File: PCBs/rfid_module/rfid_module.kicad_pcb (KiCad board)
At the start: 2 copper layers, 15.8 x 12 mm, 47 parts, among them IC201 TLV9004SIRTER, IC202 MAX9027EBT+T, Q201 DMN21D2UFB-7B, Q202 DMP21D5UFB4-7B, Q203 DMN21D2UFB-7B, Q204 DMN21D2UFB-7B

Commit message: RFID Module progress
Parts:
- added C301: 4u7, Capacitor_SMD:C_0402_1005Metric, F.Cu at (114.4, 60.9)
- added C302: 100n, Capacitor_SMD:C_0402_1005Metric, F.Cu at (113.0, 61.9)
- added C303: 1u, Capacitor_SMD:C_0402_1005Metric, B.Cu at (114.5, 60.9)
- added C304: 100n, Capacitor_SMD:C_0402_1005Metric, B.Cu at (114.5, 59.9)
- added C501: 22u, Capacitor_SMD:C_0402_1005Metric, F.Cu at (115.4, 57.7)
- added C502: 4u7, Capacitor_SMD:C_0402_1005Metric, F.Cu at (112.0, 55.9)
- added IC501: MAX17291BANT+T, watch_footprints:BGA6C40P3X2_127X87X50, F.Cu at (113.6, 56.0)
- added J401: 10-Pin_Pogo_Connector_Male, watch_footprints:10-Pin Pogo Connector Male, B.Cu at (109.6, 60.4)
- added L501: 10u, Inductor_SMD:L_TDK_MLZ1608, F.Cu at (115.4, 56.0)
- added Q401: DMN21D2UFB-7B, watch_footprints:DMN21D2UFB7B, F.Cu at (114.4, 59.9)
- added R401: 10k, Resistor_SMD:R_0402_1005Metric, F.Cu at (114.4, 58.8)
- added R402: 100k, Resistor_SMD:R_0402_1005Metric, B.Cu at (114.5, 58.4)
- added R501: 3M48, Resistor_SMD:R_0402_1005Metric, F.Cu at (110.8, 55.9)
- added R502: 402k, Resistor_SMD:R_0402_1005Metric, F.Cu at (113.4, 57.7)
- added R503: 1M, Resistor_SMD:R_0402_1005Metric, F.Cu at (111.4, 57.7)
- added R504: 100k, Resistor_SMD:R_0402_1005Metric, F.Cu at (135.4, 54.9)
- added U101: Watch_Module_Outline_V1, watch_footprints:Watch Module Outline V1, F.Cu at (105.0, 62.0)
- added U301: STM32G071G8Ux, Package_DFN_QFN:QFN-28_4x4mm_P0.5mm, F.Cu at (109.8, 61.4)
- R206: value 4R7 -> 100R
- R207: value 4R7 -> 10k
- moved Q203 64.1 mm to (107.0, 55.8), turned to -90 degrees
- moved Q202 61.5 mm to (108.4, 55.8), turned to -90 degrees
- moved Q201 58.0 mm to (109.5, 57.7), turned to 180 degrees
- moved R206 46.0 mm to (106.9, 57.7), turned to 90 degrees
- moved R204 42.5 mm to (109.6, 55.9), turned to 90 degrees
- moved R202 40.2 mm to (108.0, 57.7), turned to 90 degrees
- moved R201 39.8 mm to (106.2, 59.3)
- moved R207 39.6 mm to (114.5, 52.1), turned to 90 degrees
- moved L201 35.2 mm to (100.0, 56.5), turned to 180 degrees
- moved IC201 34.6 mm to (99.3, 64.1)
- moved IC202 22.1 mm to (151.2, 73.8)
- moved Q204 22.1 mm to (161.9, 76.6)
- moved R212 22.1 mm to (148.6, 67.0)
- moved R213 22.1 mm to (151.5, 57.0)
- moved R218 22.1 mm to (151.5, 67.0)
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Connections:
- net +VSYS renamed /Boost Converter/VRF
- Q201 pad 3: /RFID/SHIFT_G -> /RFID/GATE
- Q202 pad 1: /RFID/SHIFT_PD -> /RFID/OUT_SHIFT
- Q202 pad 2: /RFID/SHIFT_G -> /RFID/GATE
- Q203 pad 1: /RFID/SHIFT_G -> /RFID/OUTN_G
- Q203 pad 3: /RFID/SHIFT_ND -> /RFID/OUT_SHIFT
- R201 pad 2: /RFID/OUT -> /RFID/OUTN
- R202 pad 1: /RFID/OUT -> /RFID/OUTN
- R202 pad 2: /RFID/OUT_G -> /RFID/OUTN_G
- R204 pad 1: /RFID/SHIFT_G -> /RFID/GATE
- R206 pad 1: /RFID/OUT_SHIFT -> /RFID/OUT
- R206 pad 2: /RFID/SHIFT_PD -> /RFID/OUT_G
- R207 pad 1: /RFID/SHIFT_ND -> /RFID/OUT
- R207 pad 2: /RFID/OUT_SHIFT -> +3V3
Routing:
- net GND: track 0.00 -> 7.53 mm, vias 0 -> 6
- net /Boost Converter/EN: track 0.00 -> 5.92 mm
- net /Pogo Connector/LPUART1_RX: track 0.00 -> 5.55 mm, vias 0 -> 1
- net /Pogo Connector/LPUART1_RX_1V8: track 0.00 -> 5.40 mm, vias 0 -> 1
- net +1V8: track 0.00 -> 4.29 mm, vias 0 -> 1
- net /Boost Converter/FB: track 0.00 -> 4.24 mm
- net /RFID/OUT: track 0.00 -> 3.85 mm
- net /RFID/OUTN: track 0.00 -> 3.62 mm
- net /RFID/GATE: track 0.00 -> 3.38 mm
- net +3V3: track 0.00 -> 3.20 mm, vias 0 -> 3
- net /RFID/OUT_G: track 0.00 -> 2.55 mm
- net /Boost Converter/FB_OFFSET: track 0.00 -> 2.27 mm
- net /RFID/OUTN_G: track 0.00 -> 1.86 mm
- net /Pogo Connector/LPUART1_TX: track 0.00 -> 1.64 mm, vias 0 -> 1
- net /STM32G0/NRST: track 0.00 -> 1.59 mm, vias 0 -> 1
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- added copper zone on In1.Cu, net GND
- added copper zone on In3.Cu, net GND
- added copper zone on In6.Cu, net GND
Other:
- board size 15.8 x 12 mm -> 22.5 x 14.5 mm
- copper layers 2 -> 8

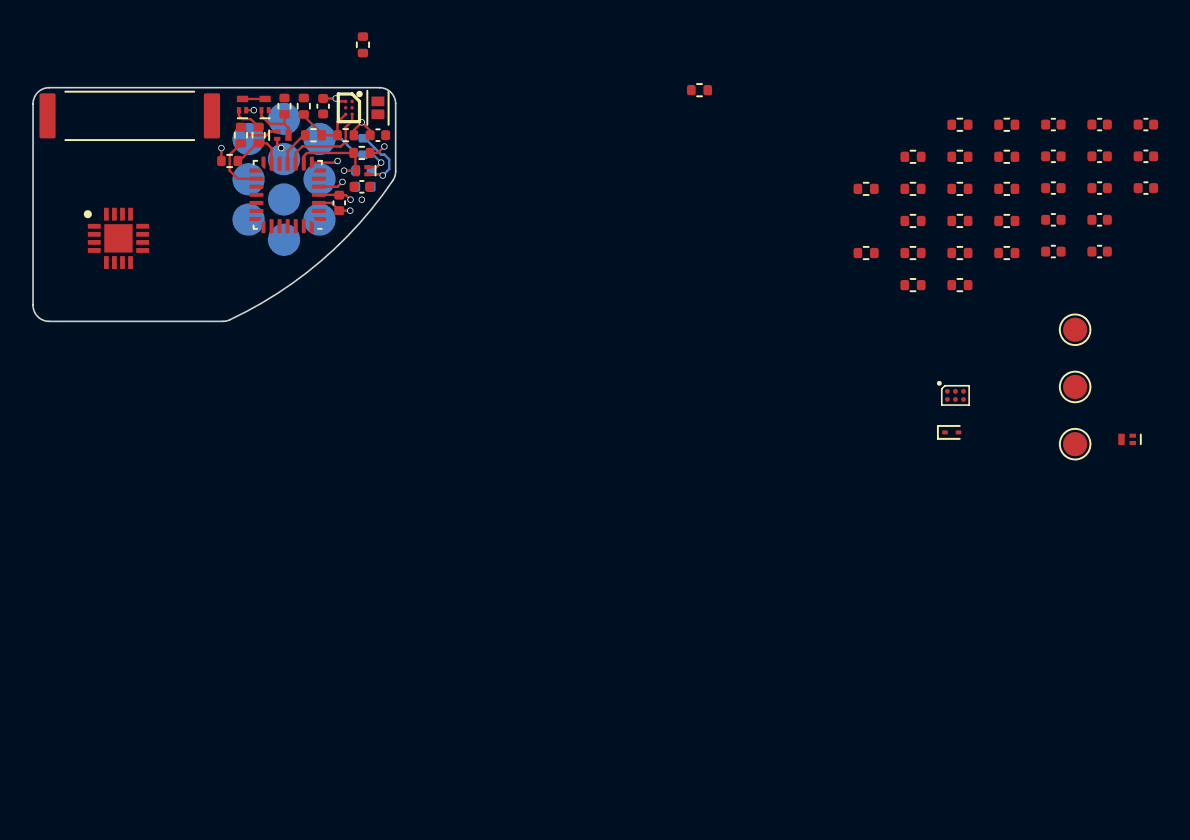
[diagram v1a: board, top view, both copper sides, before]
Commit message: RFID PCB Done, started lower flex PCB
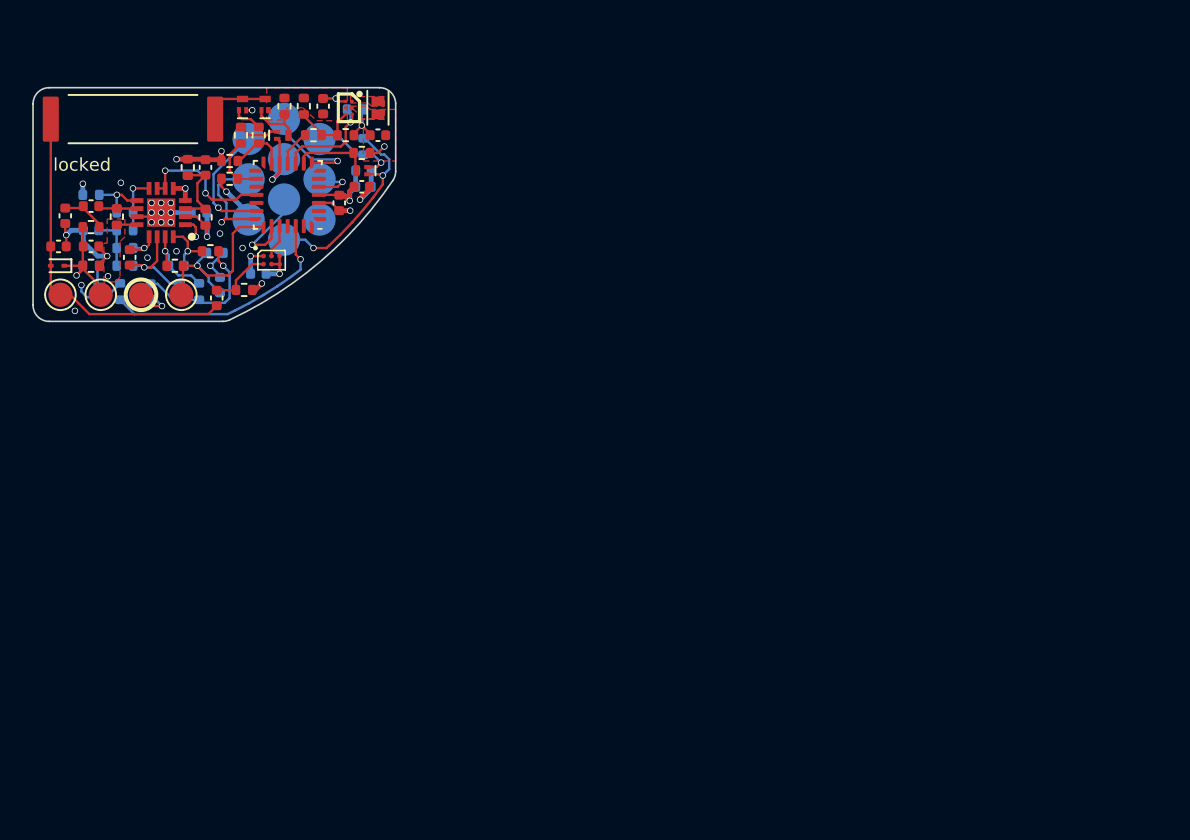
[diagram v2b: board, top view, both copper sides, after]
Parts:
- added TP101: 1.5mm, TestPoint:TestPoint_Pad_D1.5mm, F.Cu at (100.7, 67.6)
- C203, C206, C210, C211, C212, C213, Q204, R208, R209, R210, R213, R214, R215, R216, R218, R220, R223, R504: moved to B.Cu
- moved Q204 64.4 mm to (98.1, 67.4), turned to -90 degrees
- moved TP201 63.0 mm to (95.7, 67.6)
- moved C206 62.9 mm to (97.6, 63.6), turned to 180 degrees
- moved C207 62.8 mm to (97.6, 64.6)
- moved C205 61.7 mm to (95.6, 64.6)
- moved C201 61.6 mm to (96.0, 62.7), turned to -90 degrees
- moved TP202 60.7 mm to (98.2, 67.6)
- moved C212 60.5 mm to (102.9, 65.8)
- moved C208 60.3 mm to (100.0, 65.3), turned to 90 degrees
- moved C202 59.8 mm to (97.6, 62.1)
- moved C210 58.9 mm to (101.3, 67.4), turned to -90 degrees
- moved C213 57.8 mm to (105.6, 67.0), turned to 90 degrees
- moved D201 56.4 mm to (95.5, 65.8), turned to 180 degrees
- moved TP203 56.2 mm to (103.2, 67.6)
- moved C211 55.8 mm to (108.0, 66.3)
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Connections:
- C211 pad 1: +1V8 -> +3V3
- IC202 pad A1: +1V8 -> +3V3
- J401 pad A1: unconnected-(J401-PadA1) -> /Pogo Connector/SWDIO
- J401 pad A2: unconnected-(J401-PadA2) -> /Pogo Connector/SWCLK
- J401 pad B3: unconnected-(J401-PadB3) -> /Pogo Connector/IRQN
- J401 pad B4: +1V8 -> IOREF
- J401 pad C2: unconnected-(J401-PadC2) -> /Pogo Connector/NRST
- Q401 pad 1: +1V8 -> IOREF
- R402 pad 1: +1V8 -> IOREF
- U301 pad 12: unconnected-(U301-PA6-Pad12) -> GND
- U301 pad 18: unconnected-(U301-PA11/PA9-Pad18) -> /RFID/SHDN
- U301 pad 20: /STM32G0/SWDIO -> /Pogo Connector/SWDIO
- U301 pad 21: /STM32G0/SWCLK -> /Pogo Connector/SWCLK
- U301 pad 23: unconnected-(U301-PB3-Pad23) -> /Pogo Connector/IRQN
- U301 pad 26: unconnected-(U301-PB6-Pad26) -> /RFID/PULL
- U301 pad 5: /STM32G0/NRST -> /Pogo Connector/NRST
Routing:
- net GND: track 7.53 -> 36.2 mm, vias 6 -> 29
- net /RFID/RF: track 0.00 -> 21.8 mm
- net /RFID/PULL: track 0.00 -> 15.2 mm, vias 0 -> 1
- net /RFID/RF_IN: track 0.00 -> 13.0 mm, vias 0 -> 1
- net IOREF: track 0.00 -> 13.0 mm, vias 0 -> 2
- net +3V3: track 3.20 -> 15.3 mm, vias 3 -> 6
- net /RFID/AMP3_IN: track 0.00 -> 8.70 mm, vias 0 -> 1
- net /RFID/SHDN: track 0.00 -> 8.66 mm, vias 0 -> 2
- net /Pogo Connector/SWDIO: track 0.00 -> 7.74 mm, vias 0 -> 1
- net /RFID/SIGNAL_ENVELOPE: track 0.00 -> 7.36 mm, vias 0 -> 1
- net /Pogo Connector/SWCLK: track 0.00 -> 6.84 mm, vias 0 -> 1
- net /RFID/AMP2_OUT: track 0.00 -> 6.77 mm, vias 0 -> 1
- net /Pogo Connector/IRQN: track 0.00 -> 5.76 mm, vias 0 -> 1
- net /RFID/AMP3_OUT: track 0.00 -> 5.16 mm, vias 0 -> 1
- net /RFID/1V65_UNREG: track 0.00 -> 4.89 mm
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- added copper zone on F.Cu, net +1V65
- added copper zone on In2.Cu, net +1V65
- added copper zone on F.Cu, net +3V3
- added copper zone on In4.Cu, net +3V3
- added copper zone on In5.Cu, net +3V3
- added copper zone on F.Cu, net /Boost Converter/LX
- added copper zone on F.Cu, net /Boost Converter/VRF
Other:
- board text added: "locked"

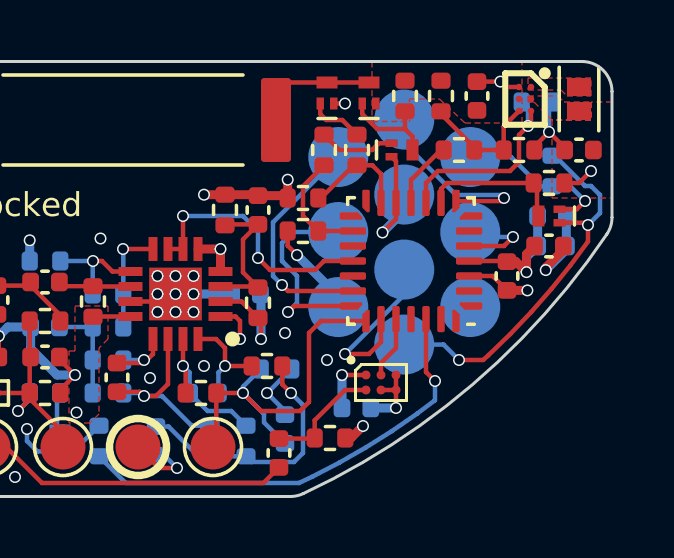
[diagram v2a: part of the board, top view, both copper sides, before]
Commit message: Flex PCB finished. Need to rotate RFID transponder coil.
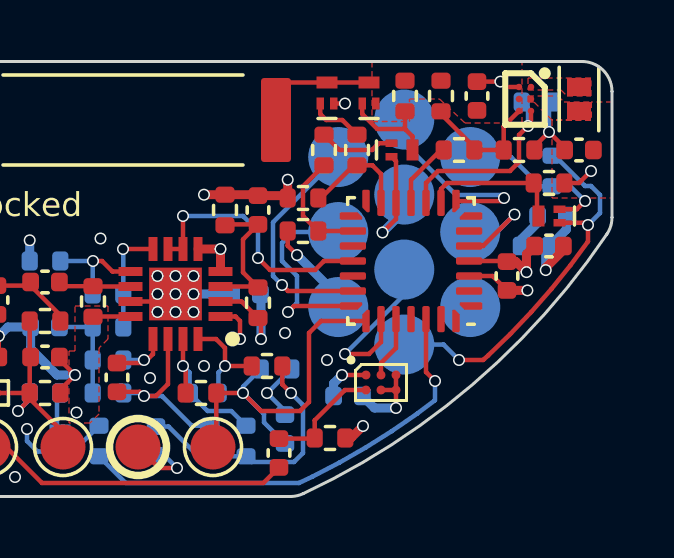
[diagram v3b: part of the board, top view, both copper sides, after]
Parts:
- moved C303 0.55 mm to (114.0, 60.9)
- moved C211 0.49 mm to (107.7, 65.9)
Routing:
- net GND: track 36.2 -> 36.8 mm
- net /Pogo Connector/NRST: track 3.08 -> 3.66 mm
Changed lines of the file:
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@@
   )
   (footprint "Capacitor_SMD:C_0402_1005Metric" locked (layer "B.Cu")
-    (at 114.5 60.9 180)
+    (at 113.95 60.9 180)
     (descr "Capacitor SMD 0402 (1005 Metric), square (rectangular) end terminal, IPC_7351 nominal, (Body size source: IPC-SM-782 page 76, https://www.pcb-3d.com/wordpress/wp-content/uploads/ipc-sm-782a_amendment_1_and_2.pdf), generated with kicad-footprint-generator")
     (tags "capacitor")
@@
   )
   (footprint "Capacitor_SMD:C_0402_1005Metric" locked (layer "B.Cu")
-    (at 107.98 66.3)
+    (at 107.7 65.9)
     (descr "Capacitor SMD 0402 (1005 Metric), square (rectangular) end terminal, IPC_7351 nominal, (Body size source: IPC-SM-782 page 76, https://www.pcb-3d.com/wordpress/wp-content/uploads/ipc-sm-782a_amendment_1_and_2.pdf), generated with kicad-footprint-generator")
     (tags "capacitor")
@@
   (via locked (at 101.95 61.9) (size 0.4) (drill 0.3) (layers "F.Cu" "B.Cu") (remove_unused_layers) (keep_end_layers) (zone_layer_connections "In1.Cu" "In3.Cu" "In6.Cu") (net 2))
   (segment locked (start 97.12 63.6) (end 96.36 63.6) (width 0.3) (layer "B.Cu") (net 2))
+  (segment locked (start 114.02 60.13) (end 114.02 59.9) (width 0.3) (layer "B.Cu") (net 2))
   (segment locked (start 97.12 63.6) (end 97.12 64.32) (width 0.3) (layer "B.Cu") (net 2))
+  (segment locked (start 113.47 60.9) (end 113.47 60.68) (width 0.3) (layer "B.Cu") (net 2))
   (segment locked (start 97 67.4) (end 97 67) (width 0.15) (layer "B.Cu") (net 2))
   (segment locked (start 97.35 67.75) (end 97 67.4) (width 0.15) (layer "B.Cu") (net 2))
@@
   (segment locked (start 101.3 67.88) (end 101.58 67.88) (width 0.15) (layer "B.Cu") (net 2))
   (segment locked (start 114.4 56.21) (end 114.51 56.1) (width 0.15) (layer "B.Cu") (net 2))
+  (segment locked (start 108.18 65.9) (end 108.58 66.3) (width 0.3) (layer "B.Cu") (net 2))
   (segment locked (start 101.58 67.88) (end 102 68.3) (width 0.15) (layer "B.Cu") (net 2))
-  (segment locked (start 108.46 66.3) (end 109.3 66.3) (width 0.3) (layer "B.Cu") (net 2))
   (segment locked (start 105 65.8) (end 105.01 65.8) (width 0.15) (layer "B.Cu") (net 2))
-  (segment locked (start 113.649 61.271) (end 114.02 60.9) (width 0.3) (layer "B.Cu") (net 2))
-  (segment locked (start 114.02 59.9) (end 114.02 60.9) (width 0.3) (layer "B.Cu") (net 2))
-  (segment locked (start 113.649 61.771) (end 113.649 61.271) (width 0.3) (layer "B.Cu") (net 2))
   (segment locked (start 109.575 59.725) (end 109.575 59.185) (width 0.3) (layer "B.Cu") (net 2))
+  (segment locked (start 113.649 61.079) (end 113.47 60.9) (width 0.3) (layer "B.Cu") (net 2))
   (segment locked (start 97.875 67.75) (end 97.35 67.75) (width 0.15) (layer "B.Cu") (net 2))
   (segment locked (start 103.82 62.5) (end 102.55 62.5) (width 0.3) (layer "B.Cu") (net 2))
+  (segment locked (start 113.649 61.771) (end 113.649 61.079) (width 0.3) (layer "B.Cu") (net 2))
   (segment locked (start 108.85 60.45) (end 109.575 59.725) (width 0.3) (layer "B.Cu") (net 2))
   (segment locked (start 105.6 66.52) (end 105.6 66.4) (width 0.15) (layer "B.Cu") (net 2))
+  (segment locked (start 108.58 66.3) (end 109.3 66.3) (width 0.3) (layer "B.Cu") (net 2))
   (segment locked (start 105.6 66.4) (end 105 65.8) (width 0.15) (layer "B.Cu") (net 2))
   (segment locked (start 105.01 65.8) (end 105.81 65) (width 0.15) (layer "B.Cu") (net 2))
+  (segment locked (start 113.47 60.68) (end 114.02 60.13) (width 0.3) (layer "B.Cu") (net 2))
   (segment locked (start 99.21 62.25) (end 99.2 62.24) (width 0.15) (layer "F.Cu") (net 3))
   (segment locked (start 98.22 62.24) (end 98.08 62.1) (width 0.15) (layer "F.Cu") (net 3))
@@
   (via locked (at 104.8 64) (size 0.4) (drill 0.3) (layers "F.Cu" "B.Cu") (remove_unused_layers) (keep_end_layers) (zone_layer_connections "In4.Cu" "In5.Cu") (net 4))
   (via locked (at 106 61.2) (size 0.4) (drill 0.3) (layers "F.Cu" "B.Cu") (remove_unused_layers) (keep_end_layers) (zone_layer_connections "In4.Cu" "In5.Cu") (net 4))
-  (segment locked (start 114.98 59.9) (end 114.98 60.9) (width 0.3) (layer "B.Cu") (net 4))
+  (segment locked (start 114.291 61.703) (end 114.291 61.039) (width 0.3) (layer "B.Cu") (net 4))
+  (segment locked (start 114.98 60.35) (end 114.98 59.9) (width 0.3) (layer "B.Cu") (net 4))
+  (segment locked (start 114.291 61.039) (end 114.98 60.35) (width 0.3) (layer "B.Cu") (net 4))
   (segment locked (start 106 61.2) (end 107.375 62.575) (width 0.3) (layer "B.Cu") (net 4))
+  (segment locked (start 107.22 65.48) (end 107.5 65.2) (width 0.3) (layer "B.Cu") (net 4))
   (segment locked (start 104.78 62.5) (end 104.8 62.52) (width 0.3) (layer "B.Cu") (net 4))
-  (segment locked (start 107.5 66.3) (end 107.5 65.2) (width 0.3) (layer "B.Cu") (net 4))
-  (segment locked (start 114.291 61.703) (end 114.98 61.014) (width 0.3) (layer "B.Cu") (net 4))
-  (segment locked (start 114.98 61.014) (end 114.98 60.9) (width 0.3) (layer "B.Cu") (net 4))
   (segment locked (start 104.8 62.52) (end 104.8 64) (width 0.3) (layer "B.Cu") (net 4))
   (segment locked (start 107.375 62.575) (end 107.375 62.935) (width 0.15) (layer "B.Cu") (net 4))
+  (segment locked (start 107.22 65.9) (end 107.22 65.48) (width 0.3) (layer "B.Cu") (net 4))
   (segment locked (start 104.67 62.25) (end 104.7 62.28) (width 0.15) (layer "F.Cu") (net 5))
   (segment locked (start 103.63 60.18) (end 103.6 60.21) (width 0.15) (layer "F.Cu") (net 5))
@@
   (segment locked (start 109.575 61.685) (end 109.575 62.523299) (width 0.15) (layer "B.Cu") (net 41))
   (segment locked (start 109.575 62.523299) (end 107.6 64.498299) (width 0.15) (layer "B.Cu") (net 41))
-  (segment locked (start 112.9 60.9) (end 113.2 60.6) (width 0.15) (layer "F.Cu") (net 42))
-  (segment locked (start 111.7375 60.9) (end 112.9 60.9) (width 0.15) (layer "F.Cu") (net 42))
-  (via locked (at 113.2 60.6) (size 0.4) (drill 0.3) (layers "F.Cu" "B.Cu") (remove_unused_layers) (keep_end_layers) (zone_layer_connections) (net 42))
-  (segment locked (start 111.94 60.6) (end 111.775 60.435) (width 0.15) (layer "B.Cu") (net 42))
-  (segment locked (start 113.2 60.6) (end 111.94 60.6) (width 0.15) (layer "B.Cu") (net 42))
+  (segment locked (start 112.2 60.9) (end 111.7375 60.9) (width 0.15) (layer "F.Cu") (net 42))
+  (segment locked (start 113.25 59.85) (end 112.2 60.9) (width 0.15) (layer "F.Cu") (net 42))
+  (via locked (at 113.25 59.85) (size 0.4) (drill 0.3) (layers "F.Cu" "B.Cu") (remove_unused_layers) (keep_end_layers) (zone_layer_connections) (net 42))
+  (segment locked (start 112.665 60.435) (end 111.775 60.435) (width 0.15) (layer "B.Cu") (net 42))
+  (segment locked (start 113.25 59.85) (end 112.665 60.435) (width 0.15) (layer "B.Cu") (net 42))
   (segment locked (start 115.7 60.750583) (end 115.7 60.2) (width 0.15) (layer "F.Cu") (net 43))
   (segment locked (start 113.807143 63.101736) (end 114.479452 62.333193) (width 0.15) (layer "F.Cu") (net 43))
